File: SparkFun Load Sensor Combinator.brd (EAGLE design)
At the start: 27.9 x 17.8 mm, 12 parts

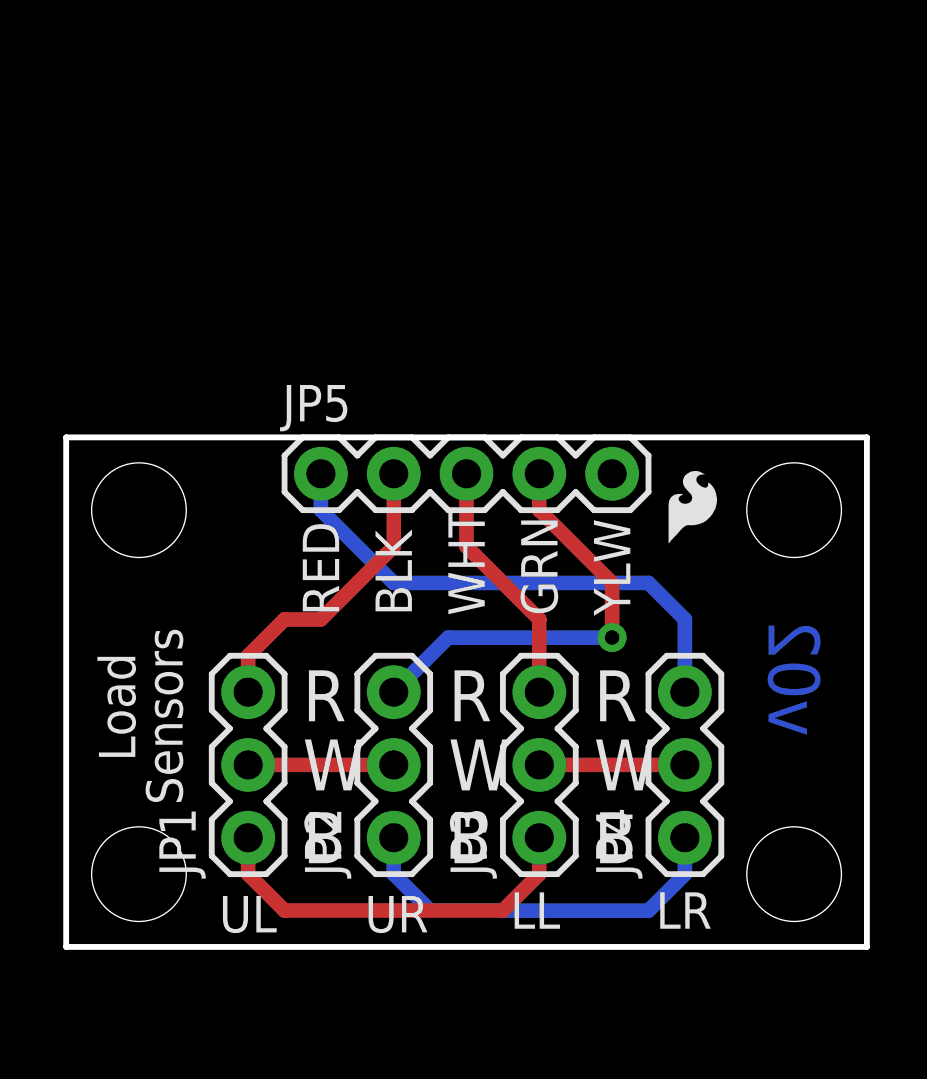
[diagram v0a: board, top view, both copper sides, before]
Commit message: Added RJ45
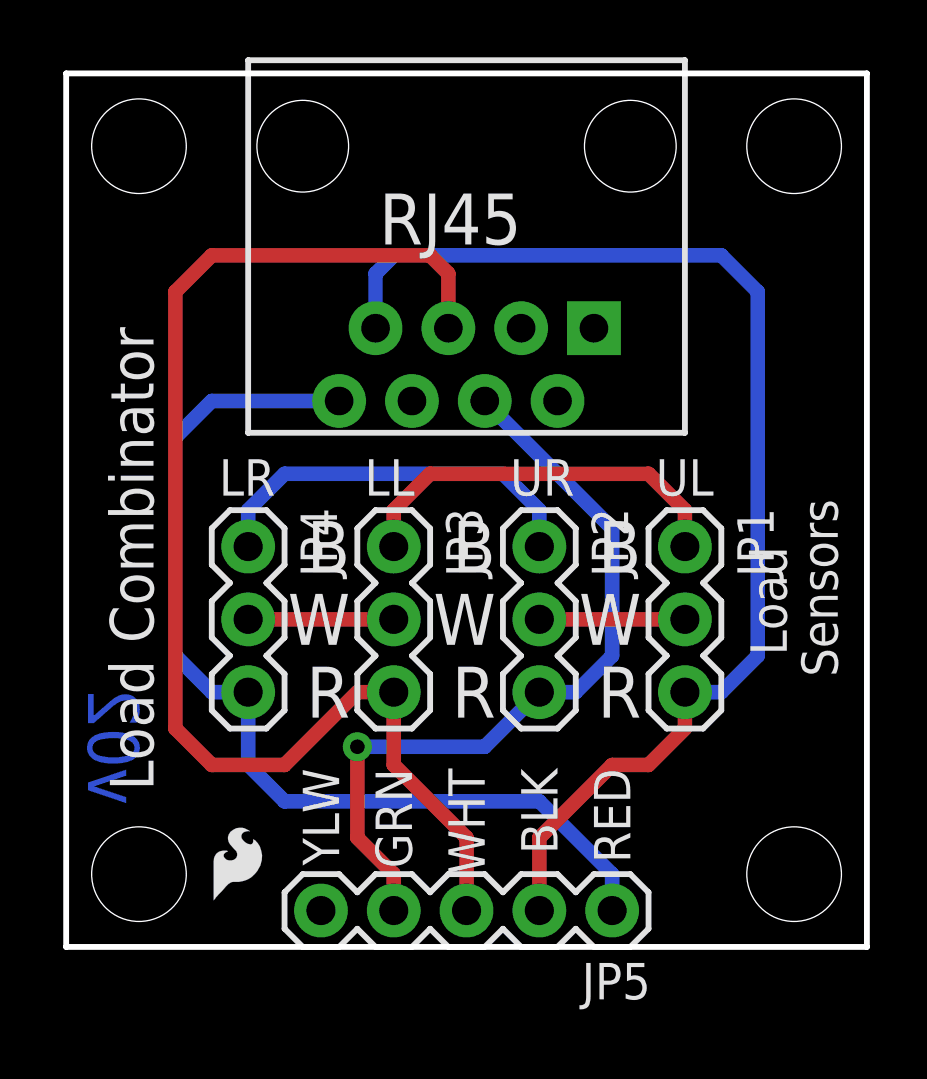
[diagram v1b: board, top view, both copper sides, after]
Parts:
- added JP6: RJ45, SparkFun-Connectors:RJ45-8
- moved STANDOFF1 34.2 mm to (25.4, 27.9), turned to 180 degrees
- moved STANDOFF2 34.2 mm to (2.54, 27.9), turned to 180 degrees
- moved STANDOFF3 26.2 mm to (25.4, 2.54), turned to 180 degrees
- moved STANDOFF4 26.2 mm to (2.54, 2.54), turned to 180 degrees
- moved LOGO3 20.2 mm to (4.83, 1.27)
- moved U$7 19.8 mm to (21.6, 2.54)
- moved JP5 18.3 mm to (19.1, 1.27), turned to 180 degrees
- moved JP1 18.3 mm to (21.6, 14.0), turned to 270 degrees
- moved JP4 18.3 mm to (6.35, 14.0), turned to 270 degrees
- moved JP2 11.4 mm to (16.5, 14.0), turned to 270 degrees
- moved JP3 11.4 mm to (11.4, 14.0), turned to 270 degrees
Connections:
- net A+: now also JP6.5
- net A-: now also JP6.4
- net E+: now also JP6.8
- net E-: now also JP6.7
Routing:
- net A+: track 8.67 -> 45.3 mm
- net E-: track 10.5 -> 42.3 mm
- net E+: track 18.1 -> 35.0 mm
- net A-: track 15.2 -> 27.2 mm
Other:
- board size 27.9 x 17.8 mm -> 27.9 x 30.5 mm
- board text added: "N. Seidle"
- board text added: "RJ45"
